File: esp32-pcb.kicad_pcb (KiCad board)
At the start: 2 copper layers, 25.2 x 59.4 mm, 48 parts, among them J1 Conn_01x15_Male, J2 Conn_01x15_Male, Q1 SI2333DDS-T1-GE3, Q2 BSS138Q-7-F, Q3 MMBT3904, Q4 MMBT3904, SW1 RESET, SW2 USER, SW3 SW_DIP_x04, U1 TLV75533, U2 ESP32-WROOM-32, U3 CP2102N-A01-GQFN24

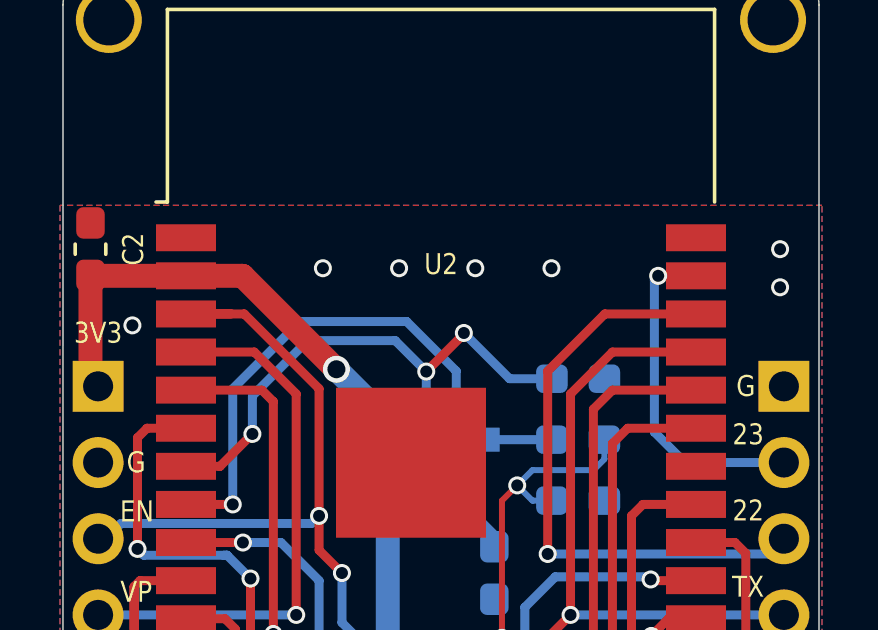
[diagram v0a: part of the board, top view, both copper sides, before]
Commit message: Add 4.7uF capacitor between EN and GND to ensure EN rising edge is slow
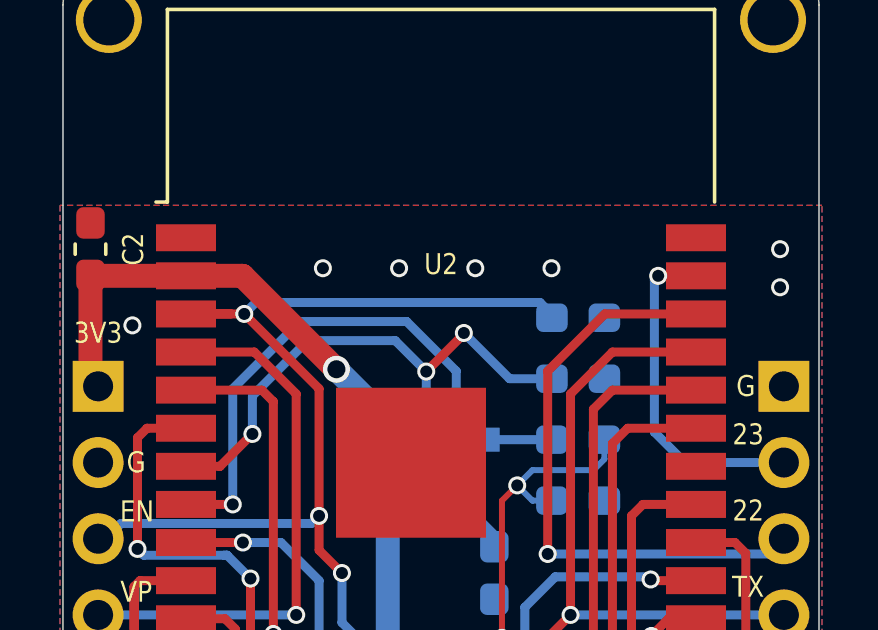
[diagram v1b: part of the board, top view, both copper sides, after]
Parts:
- added C8: 4.7uF, Capacitor_SMD:C_0603_1608Metric_Pad1.05x0.95mm_HandSolder, B.Cu at (146.3, 79.8)
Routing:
- net ESP_EN: track 65.7 -> 76.4 mm, vias 7 -> 8
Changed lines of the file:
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@@
     (thickness 1.6)
     (drawings 3056)
-    (tracks 607)
+    (tracks 612)
     (zones 0)
-    (modules 48)
+    (modules 49)
     (nets 74)
   )
@@
     (add_net V_BAT_MEASURE)
   )
+  (module Capacitor_SMD:C_0603_1608Metric_Pad1.05x0.95mm_HandSolder (layer B.Cu)
+    (at 146.304 79.756)
+    (descr "Capacitor SMD 0603 (1608 Metric), square (rectangular) end terminal, IPC_7351 nominal with elongated pad for handsoldering. (Body size source: http://www.tortai-tech.com/upload/download/2011102023233369053.pdf), generated with kicad-footprint-generator")
+    (tags "capacitor handsolder")
+    (attr smd)
+    (fp_text reference C8 (at 2.54 0) (layer B.SilkS)
+      (effects (font (size 0.7 0.6) (thickness 0.15)) (justify mirror))
+    )
+    (fp_text value 4.7uF (at 0 -1.43) (layer B.Fab)
+      (effects (font (size 1 1) (thickness 0.15)) (justify mirror))
+    )
+    (fp_text user %R (at 0 0) (layer B.Fab)
+      (effects (font (size 0.4 0.4) (thickness 0.06)) (justify mirror))
+    )
+    (fp_line (start 1.65 -0.73) (end -1.65 -0.73) (layer B.CrtYd) (width 0.05))
+    (fp_line (start 1.65 0.73) (end 1.65 -0.73) (layer B.CrtYd) (width 0.05))
+    (fp_line (start -1.65 0.73) (end 1.65 0.73) (layer B.CrtYd) (width 0.05))
+    (fp_line (start -1.65 -0.73) (end -1.65 0.73) (layer B.CrtYd) (width 0.05))
+    (fp_line (start -0.171267 -0.51) (end 0.171267 -0.51) (layer B.SilkS) (width 0.12))
+    (fp_line (start -0.171267 0.51) (end 0.171267 0.51) (layer B.SilkS) (width 0.12))
+    (fp_line (start 0.8 -0.4) (end -0.8 -0.4) (layer B.Fab) (width 0.1))
+    (fp_line (start 0.8 0.4) (end 0.8 -0.4) (layer B.Fab) (width 0.1))
+    (fp_line (start -0.8 0.4) (end 0.8 0.4) (layer B.Fab) (width 0.1))
+    (fp_line (start -0.8 -0.4) (end -0.8 0.4) (layer B.Fab) (width 0.1))
+    (pad 2 smd roundrect (at 0.875 0) (size 1.05 0.95) (layers B.Cu B.Paste B.Mask) (roundrect_rratio 0.25)
+      (net 1 GND))
+    (pad 1 smd roundrect (at -0.875 0) (size 1.05 0.95) (layers B.Cu B.Paste B.Mask) (roundrect_rratio 0.25)
+      (net 25 ESP_EN))
+    (model ${KISYS3DMOD}/Capacitor_SMD.3dshapes/C_0603_1608Metric.wrl
+      (at (xyz 0 0 0))
+      (scale (xyz 1 1 1))
+      (rotate (xyz 0 0 0))
+    )
+  )
   (module Package_TO_SOT_SMD:SOT-23 (layer F.Cu)
     (at 141.605 116.84 180)
@@
   (via (at 139.192 104.14) (size 0.7) (drill 0.3) (layers F.Cu B.Cu) (net 1))
   (via (at 144.272 103.632) (size 0.7) (drill 0.3) (layers F.Cu B.Cu) (net 1))
-  (via (at 137.795 78.105) (size 0.6) (drill 0.4) (layers F.Cu B.Cu) (net 1))
   (via (at 140.335 78.105) (size 0.6) (drill 0.4) (layers F.Cu B.Cu) (net 1))
   (via (at 142.875 78.105) (size 0.6) (drill 0.4) (layers F.Cu B.Cu) (net 1))
@@
   (via (at 133.35 125.73) (size 0.6) (drill 0.4) (layers F.Cu B.Cu) (net 1))
   (via (at 130.175 122.555) (size 0.6) (drill 0.4) (layers F.Cu B.Cu) (net 1))
+  (via (at 137.795 78.105) (size 0.6) (drill 0.4) (layers F.Cu B.Cu) (net 1))
   (via (at 144.272 85.344) (size 0.6) (drill 0.4) (layers F.Cu B.Cu) (net 2))
   (via (at 143.764 90.424) (size 0.6) (drill 0.4) (layers F.Cu B.Cu) (net 2))
@@
   (segment (start 138.43 89.916) (end 139.192 90.678) (width 0.3) (layer B.Cu) (net 25))
   (segment (start 139.192 95.758) (end 137.922 97.028) (width 0.3) (layer B.Cu) (net 25))
+  (segment (start 145.429 79.756) (end 145.429 79.643) (width 0.3) (layer B.Cu) (net 25))
+  (segment (start 145.429 79.643) (end 145.034 79.248) (width 0.3) (layer B.Cu) (net 25))
+  (via (at 135.174227 79.629) (size 0.6) (drill 0.4) (layers F.Cu B.Cu) (net 25))
+  (segment (start 145.034 79.248) (end 135.555227 79.248) (width 0.3) (layer B.Cu) (net 25))
+  (segment (start 135.555227 79.248) (end 135.174227 79.629) (width 0.3) (layer B.Cu) (net 25))
   (via (at 148.59 107.95) (size 0.6) (drill 0.4) (layers F.Cu B.Cu) (net 26))
   (via (at 149.86 119.38) (size 0.6) (drill 0.4) (layers F.Cu B.Cu) (net 26))

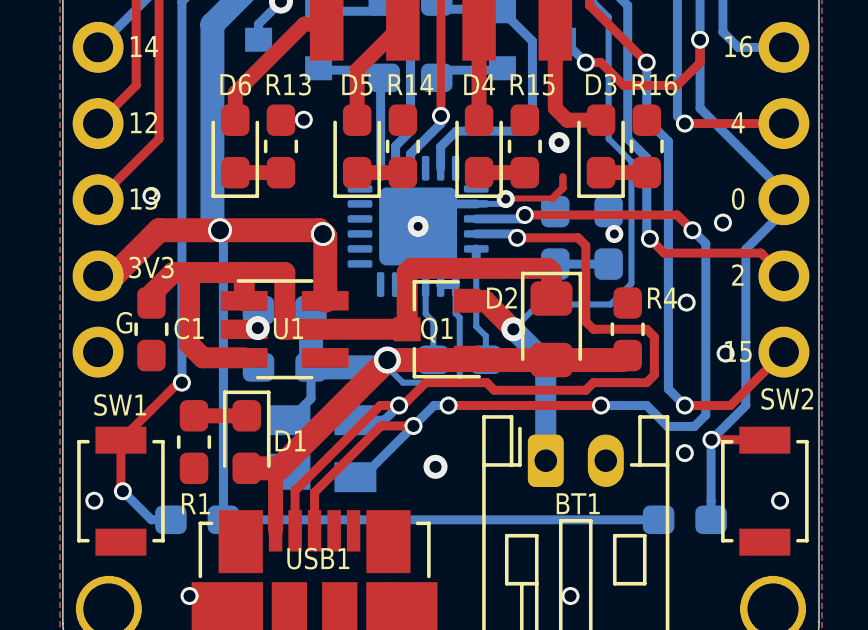
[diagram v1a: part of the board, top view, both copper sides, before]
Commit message: Fix battery protection circuit by swapping terminals of p-MOS
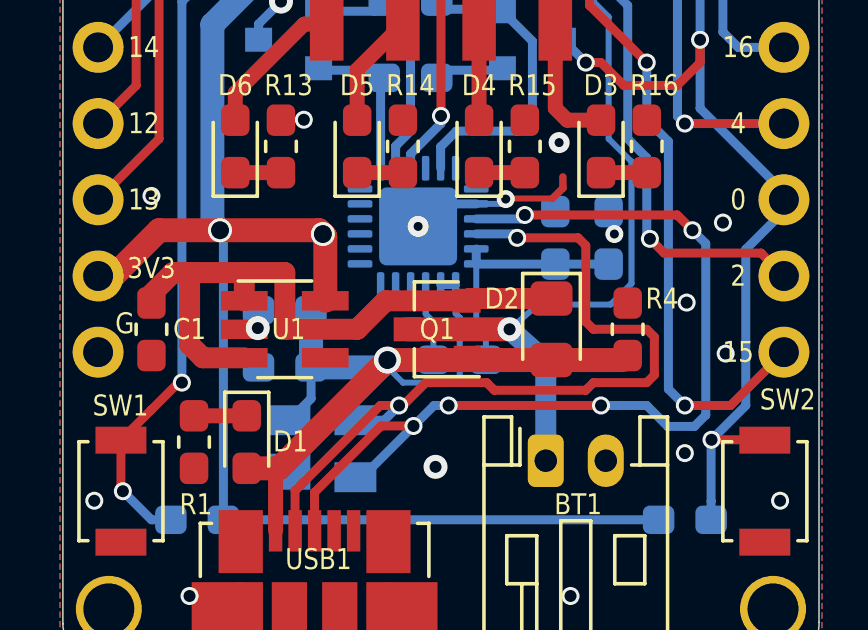
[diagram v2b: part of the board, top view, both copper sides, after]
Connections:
- Q1 pad 2: V_BAT -> Net-(C1-Pad1)
- Q1 pad 3: Net-(C1-Pad1) -> V_BAT
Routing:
- net Net-(C1-Pad1): track 24.0 -> 21.6 mm
- net V_BAT: track 48.6 -> 50.3 mm
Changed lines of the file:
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@@
     (thickness 1.6)
     (drawings 3056)
-    (tracks 612)
+    (tracks 610)
     (zones 0)
     (modules 49)
@@
   )
   (setup
-    (last_trace_width 0.25)
+    (last_trace_width 0.7)
     (user_trace_width 0.2)
     (user_trace_width 0.25)
@@
     )
     (pad 3 smd rect (at 1 0 180) (size 0.9 0.8) (layers F.Cu F.Paste F.Mask)
-      (net 73 "Net-(C1-Pad1)"))
-    (pad 2 smd rect (at -1 0.95 180) (size 0.9 0.8) (layers F.Cu F.Paste F.Mask)
       (net 2 V_BAT))
+    (pad 2 smd rect (at -1 0.95 180) (size 0.9 0.8) (layers F.Cu F.Paste F.Mask)
+      (net 73 "Net-(C1-Pad1)"))
     (pad 1 smd rect (at -1 -0.95 180) (size 0.9 0.8) (layers F.Cu F.Paste F.Mask)
       (net 5 5V_USB))
@@
   (segment (start 144.78 85.852) (end 144.272 85.344) (width 0.2) (layer B.Cu) (net 2))
   (segment (start 145.429 85.852) (end 144.78 85.852) (width 0.2) (layer B.Cu) (net 2) (status 10))
-  (segment (start 145.2245 117.9195) (end 145.2245 121.2215) (width 0.7) (layer B.Cu) (net 2))
-  (segment (start 144.145 116.84) (end 145.2245 117.9195) (width 0.7) (layer B.Cu) (net 2))
-  (segment (start 144.145 116.84) (end 143.195 115.89) (width 0.7) (layer F.Cu) (net 2))
-  (via (at 144.145 116.84) (size 0.8) (drill 0.4) (layers F.Cu B.Cu) (net 2))
-  (segment (start 143.195 115.89) (end 142.605 115.89) (width 0.7) (layer F.Cu) (net 2))
-  (segment (start 146.812 96.012) (end 144.018 93.218) (width 0.2) (layer B.Cu) (net 2))
-  (segment (start 146.812 105.918) (end 146.812 96.012) (width 0.2) (layer B.Cu) (net 2))
-  (segment (start 147.32 106.426) (end 146.812 105.918) (width 0.2) (layer B.Cu) (net 2))
-  (segment (start 144.9705 116.0145) (end 147.3835 116.0145) (width 0.2) (layer B.Cu) (net 2))
   (segment (start 144.018 93.218) (end 144.018 90.678) (width 0.2) (layer B.Cu) (net 2))
+  (segment (start 146.812 96.012) (end 144.018 93.218) (width 0.2) (layer B.Cu) (net 2))
   (segment (start 147.32 110.49) (end 147.32 106.426) (width 0.2) (layer B.Cu) (net 2))
-  (segment (start 144.145 116.84) (end 144.9705 116.0145) (width 0.2) (layer B.Cu) (net 2))
-  (segment (start 147.3835 116.0145) (end 148.082 115.316) (width 0.2) (layer B.Cu) (net 2))
+  (segment (start 148.082 111.252) (end 147.32 110.49) (width 0.2) (layer B.Cu) (net 2))
+  (segment (start 147.32 106.426) (end 146.812 105.918) (width 0.2) (layer B.Cu) (net 2))
+  (segment (start 144.018 116.84) (end 145.2245 117.9195) (width 0.7) (layer B.Cu) (net 2))
+  (via (at 144.018 116.84) (size 0.8) (drill 0.4) (layers F.Cu B.Cu) (net 2))
+  (segment (start 146.812 105.918) (end 146.812 96.012) (width 0.2) (layer B.Cu) (net 2))
+  (segment (start 144.018 116.84) (end 144.9705 116.0145) (width 0.2) (layer B.Cu) (net 2))
+  (segment (start 144.018 116.84) (end 140.605 116.84) (width 0.8) (layer F.Cu) (net 2))
   (segment (start 148.082 115.316) (end 148.082 111.252) (width 0.2) (layer B.Cu) (net 2))
+  (segment (start 144.9705 116.0145) (end 147.3835 116.0145) (width 0.2) (layer B.Cu) (net 2))
   (segment (start 144.018 90.678) (end 143.764 90.424) (width 0.2) (layer B.Cu) (net 2))
-  (segment (start 148.082 111.252) (end 147.32 110.49) (width 0.2) (layer B.Cu) (net 2))
+  (segment (start 145.2245 117.9195) (end 145.2245 121.2215) (width 0.7) (layer B.Cu) (net 2))
+  (segment (start 147.3835 116.0145) (end 148.082 115.316) (width 0.2) (layer B.Cu) (net 2))
   (segment (start 130.062 78.359) (end 130.048 78.345) (width 0.8) (layer F.Cu) (net 3) (status 30))
   (segment (start 133.232 78.359) (end 130.062 78.359) (width 0.8) (layer F.Cu) (net 3) (status 30))
@@
   (segment (start 147.32 114.667) (end 145.542 114.667) (width 0.3) (layer B.Cu) (net 4) (status 30))
   (segment (start 135.255 121.525) (end 136.285 121.525) (width 0.5) (layer F.Cu) (net 5) (status 10))
-  (segment (start 145.415 117.865) (end 139.945 117.865) (width 0.8) (layer F.Cu) (net 5) (status 10))
   (segment (start 137.4 118.11) (end 137.4 116.205) (width 0.8) (layer B.Cu) (net 5) (status 30))
   (via (at 139.945 117.865) (size 0.9) (drill 0.6) (layers F.Cu B.Cu) (net 5))
@@
   (segment (start 137.4 119.15) (end 136.68 119.87) (width 0.3) (layer B.Cu) (net 5))
   (segment (start 137.4 118.11) (end 137.4 119.15) (width 0.3) (layer B.Cu) (net 5))
+  (segment (start 145.415 117.865) (end 139.945 117.865) (width 0.8) (layer F.Cu) (net 5) (status 10))
   (segment (start 133.5 119.725) (end 135.255 119.725) (width 0.5) (layer F.Cu) (net 6) (status 30))
   (segment (start 147.066 109.869) (end 145.937 109.869) (width 0.5) (layer F.Cu) (net 7) (status 10))
@@
   (segment (start 139.107883 121.77) (end 140.814952 120.062931) (width 0.3) (layer B.Cu) (net 70))
   (segment (start 138.88 121.77) (end 139.107883 121.77) (width 0.3) (layer B.Cu) (net 70))
-  (segment (start 145.288 114.808) (end 140.748 114.808) (width 0.7) (layer F.Cu) (net 73))
   (segment (start 132.08 115.965) (end 132.08 115.67) (width 0.5) (layer F.Cu) (net 73) (status 30))
   (segment (start 132.08 115.67) (end 132.8 114.95) (width 0.7) (layer F.Cu) (net 73) (status 10))
-  (segment (start 136.525 116.84) (end 140.605 116.84) (width 0.7) (layer F.Cu) (net 73) (status 20))
   (segment (start 136.525 114.95) (end 136.525 116.84) (width 0.7) (layer F.Cu) (net 73))
   (segment (start 135.175 115.89) (end 135.175 114.95) (width 0.7) (layer F.Cu) (net 73) (status 10))
@@
   (segment (start 135.175 117.79) (end 133.792 117.79) (width 0.7) (layer F.Cu) (net 73) (status 10))
   (segment (start 133.792 117.79) (end 133.35 117.348) (width 0.7) (layer F.Cu) (net 73))
-  (segment (start 145.415 114.935) (end 145.288 114.808) (width 0.7) (layer F.Cu) (net 73))
-  (segment (start 145.415 115.815) (end 145.415 114.935) (width 0.7) (layer F.Cu) (net 73))
   (segment (start 132.8 114.95) (end 136.525 114.95) (width 0.7) (layer F.Cu) (net 73))
-  (segment (start 140.605 114.951) (end 140.605 116.84) (width 0.7) (layer F.Cu) (net 73))
-  (segment (start 140.748 114.808) (end 140.605 114.951) (width 0.7) (layer F.Cu) (net 73))
+  (segment (start 142.68 115.815) (end 142.605 115.89) (width 0.7) (layer F.Cu) (net 73))
+  (segment (start 145.415 115.815) (end 142.68 115.815) (width 0.7) (layer F.Cu) (net 73))
+  (segment (start 142.605 115.89) (end 139.888 115.89) (width 0.7) (layer F.Cu) (net 73))
+  (segment (start 138.938 116.84) (end 136.525 116.84) (width 0.7) (layer F.Cu) (net 73))
+  (segment (start 139.888 115.89) (end 138.938 116.84) (width 0.7) (layer F.Cu) (net 73))
   (zone (net 1) (net_name GND) (layer B.Cu) (hatch edge 0.508)
     (connect_pads yes (clearance 0.25))

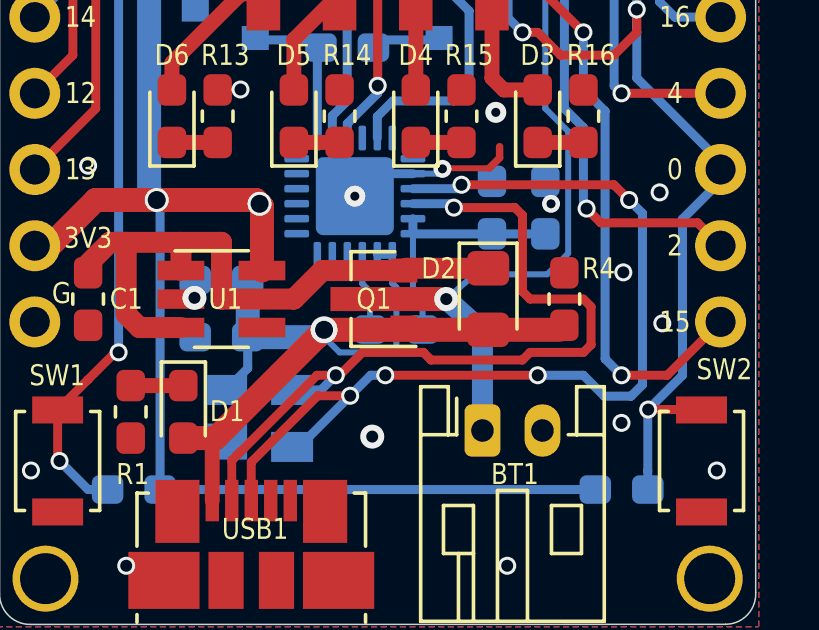
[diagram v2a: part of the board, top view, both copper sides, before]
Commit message: Use B140HW-7 Schottky diode instead of SD0805S020S1R0. The new diode has much lower guaranteed reverse current of 40µA rather than 0.2mA
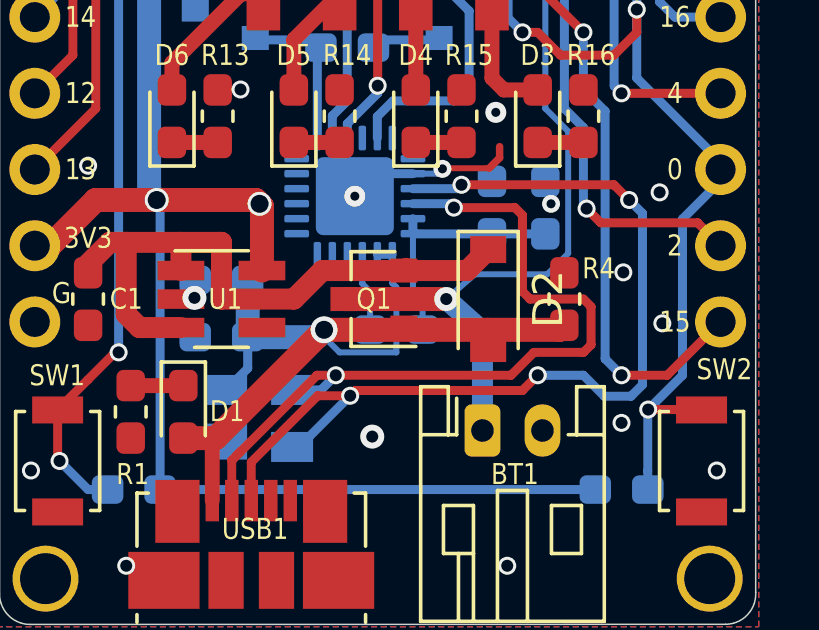
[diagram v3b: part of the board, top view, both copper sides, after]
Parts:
- D2: value D_Schottky -> B140HW-7; footprint Diode_SMD:D_0805_2012Metric_Pad1.15x1.40mm_HandSolder -> Diode_SMD:D_SOD-123
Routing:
- net 5V_USB: track 30.4 -> 31.3 mm
- net USB_D+: vias 5 -> 4

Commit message: Use larger resistors for blue LEDs
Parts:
- R1: value 1k -> 2k
- R14: value 220 -> 470
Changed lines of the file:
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@@
   )
   (setup
-    (last_trace_width 0.8)
+    (last_trace_width 0.25)
     (user_trace_width 0.2)
     (user_trace_width 0.25)
@@
       (effects (font (size 0.7 0.6) (thickness 0.16)))
     )
-    (fp_text value 220 (at 0 1.43 90) (layer F.Fab)
+    (fp_text value 470 (at 0 1.43 90) (layer F.Fab)
       (effects (font (size 1 1) (thickness 0.15)))
     )
@@
       (effects (font (size 0.7 0.6) (thickness 0.16)))
     )
-    (fp_text value 1k (at 0 1.43 270) (layer F.Fab)
-      (effects (font (size 1 1) (thickness 0.15)))
-    )
+    (fp_text value 2k (at 0 1.43 270) (layer F.Fab)
+      (effects (font (size 1 1) (thickness 0.15)))
+    )

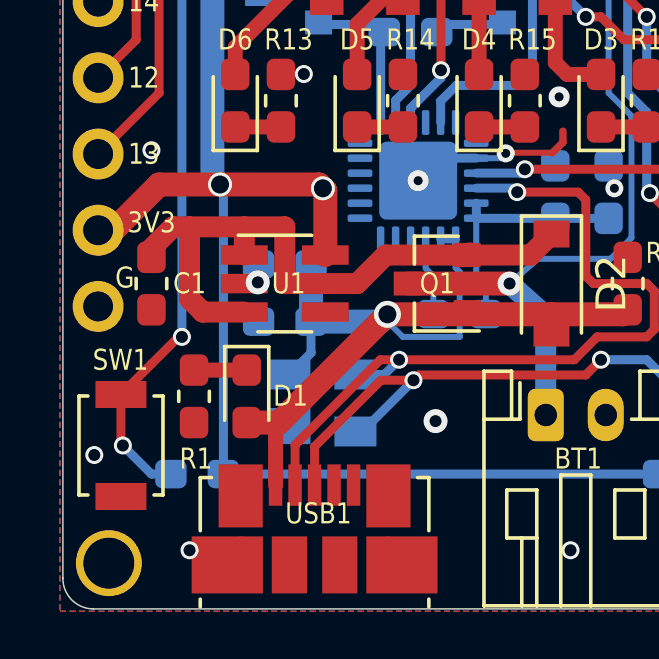
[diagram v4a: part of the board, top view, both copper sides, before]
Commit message: Turn off USB PWR led when the board is under reset
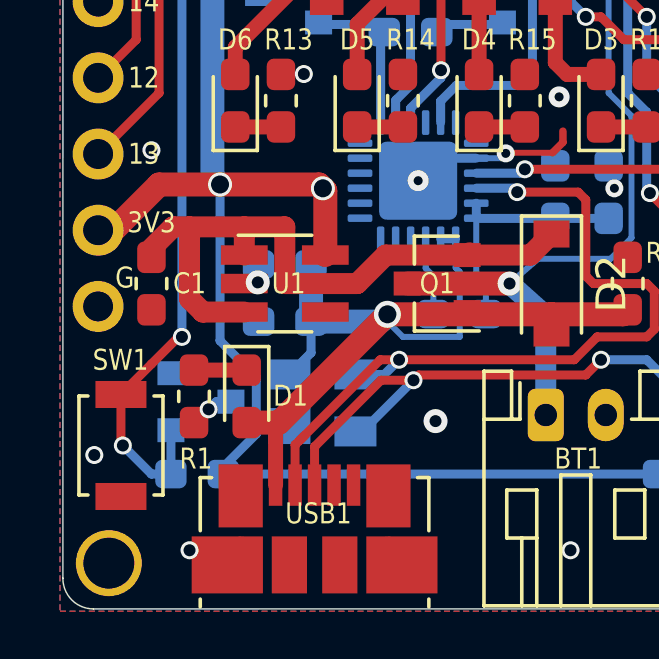
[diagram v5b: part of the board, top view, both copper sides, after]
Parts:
- added Q5: BSS138Q-7-F, Package_TO_SOT_SMD:SOT-23, B.Cu at (133.7, 120.8)
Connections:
- net ESP_EN renamed EN
- R1 pad 2: GND -> Net-(Q5-Pad3)
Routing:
- net Net-(Q5-Pad3): track 0.00 -> 1.52 mm, vias 0 -> 1
- net EN: track 76.4 -> 77.9 mm
- net 3V3: track 83.2 -> 84.3 mm
